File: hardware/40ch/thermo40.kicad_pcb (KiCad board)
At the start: 4 copper layers, 250 x 145 mm, 731 parts, among them J1001 PT100 1-2 (A B C), J1002 PT100 3 (A B C), J101 TC CH1-4, J102 TC CH5-8, J201 TC CH9-12, J202 TC CH13-16, J301 TC CH17-20, J302 TC CH21-24, J401 ENGINE REF FEED/SENSE, J501 AVR ISP, J502 LCD 20x4 HEADER, J503 PANEL BUTTONS, J601 24V IN, J701 TRIP C-NO-NC, J702 ALM C-NO-NC, J703 RS485 A B GND, J801 TC CH25-28, J802 TC CH29-32, J901 TC CH33-36, J902 TC CH37-40, K701 G6K-2F-Y DC5, K702 G6K-2F-Y DC5, Q401 2N7002, Q402 MMBT3906, Q701 2N7002, Q702 2N7002, SW501 UP, SW502 DOWN, SW503 SET, SW504 ESC, SW505 ACK, U1001 AD7124-8BCPZ, U101 AD7124-8BCPZ, U102 TMP126DCKR, U103 TMP126DCKR, U201 AD7124-8BCPZ, U202 TMP126DCKR, U203 TMP126DCKR, U301 AD7124-8BCPZ, U302 TMP126DCKR, U303 TMP126DCKR, U401 B0505S-1WR2, U402 LP2985IM5X-3.3, U403 CA-IS3761HW, U404 CA-IS3761HW, U406 REF3030AIDBZR, U407 MCP6001T-I/OT, U408 TLV7031DBVR, U409 TL431, U410 74HC154, U411 74LVC1G125, U501 ATmega1284P-AU, U601 LM5164DDAR, U703 ADM2587EBRWZ, U801 AD7124-8BCPZ, U802 TMP126DCKR, U803 TMP126DCKR, U901 AD7124-8BCPZ, U902 TMP126DCKR, U903 TMP126DCKR, Y501 8MHz

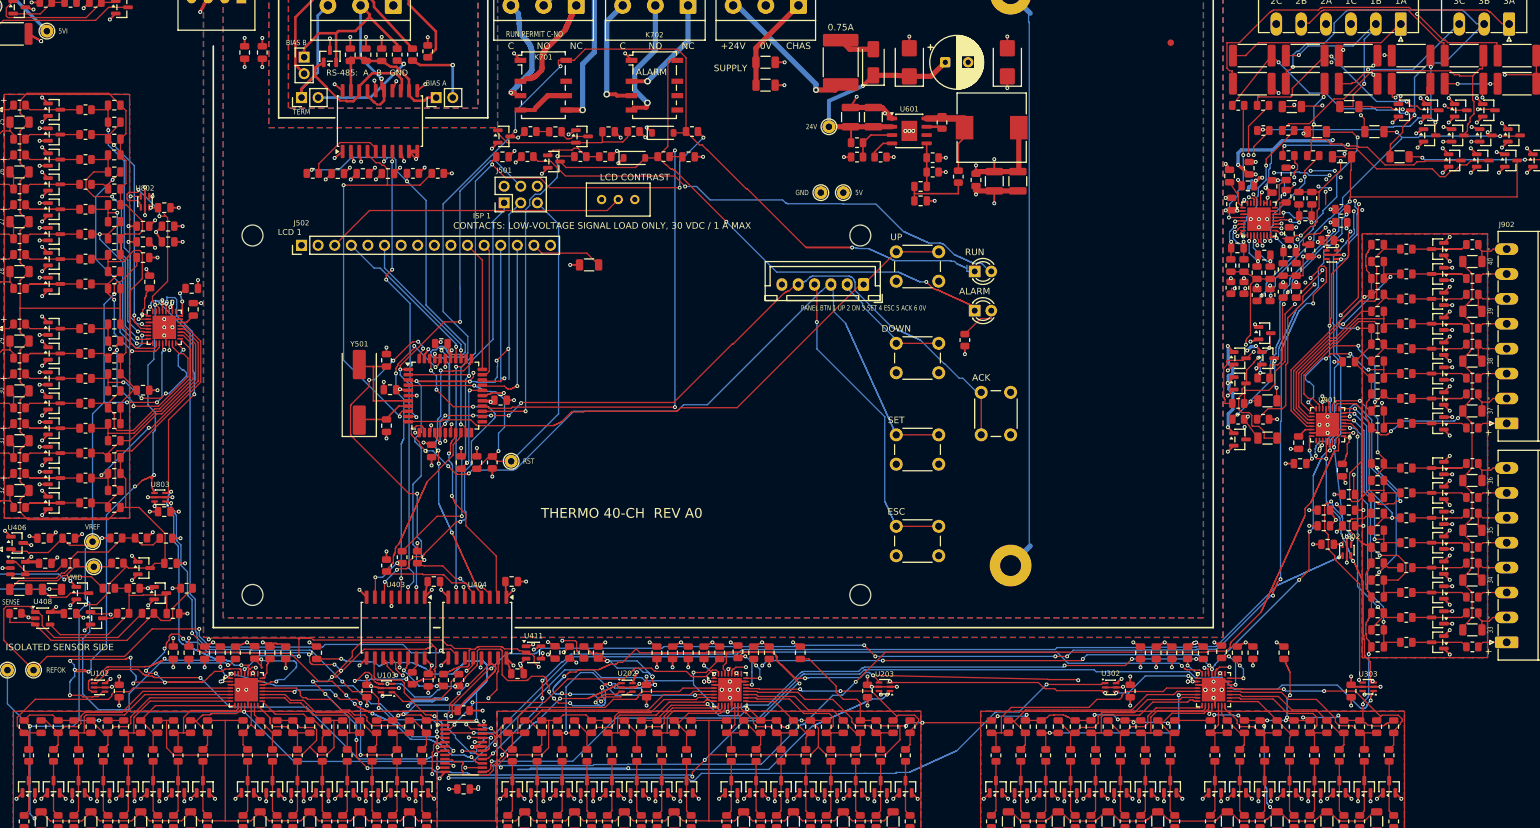
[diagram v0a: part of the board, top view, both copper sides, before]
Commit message: 40ch REV A0: drill-hole overlaps and via holes in SMD lands fixed (Astra re-review)
Sol round 11: hole pairs under 0.25 mm 19 -> 0 (KiCad hole_to_hole/holes_co_located 0),
via hole to small SMD land under 0.10 mm 61 -> 0, SAC/SBC partly shortened. DRC 0/0/0,
pincaps 0. Release 40ch-reva0-20261019-040422-9bed30; 024508 archived.

Co-Authored-By: Claude Opus 5.5 <noreply@anthropic.com>
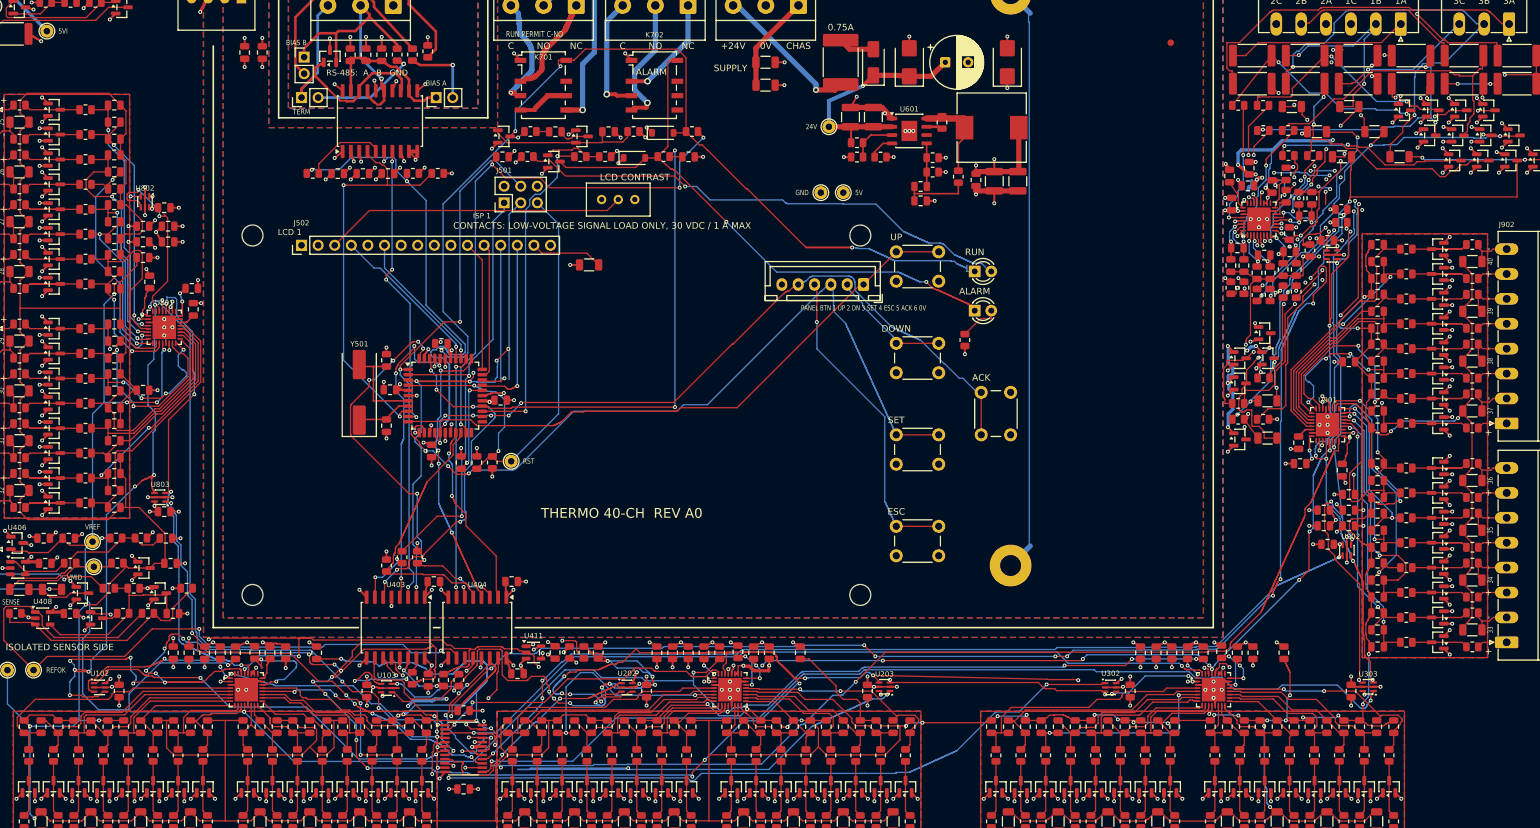
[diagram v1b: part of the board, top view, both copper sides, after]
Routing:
- net +3V3_ISO: track 352.1 -> 363.3 mm, vias 185 -> 180
- net /RTD_1/RTD1_SAC: track 66.1 -> 61.5 mm, vias 3 -> 6
- net GND_ISO: track 456.6 -> 460.3 mm, vias 239 -> 230
- net RTD3_SP: track 12.5 -> 15.5 mm
- net /RTD_1/RTD2_SBC: track 54.9 -> 57.4 mm
- net DOUT_ISO: track 506.8 -> 508.9 mm, vias 36 -> 30
- net SCLK_ISO: track 648.2 -> 650.0 mm
- net CSA1: track 44.7 -> 46.3 mm
- net /RTD_1/RTD1_C: track 5.93 -> 7.48 mm
- net V_BIAS: track 1024.9 -> 1026.4 mm, vias 39 -> 38
- net CSA0: track 44.7 -> 46.1 mm
- net RTD3_SN: track 13.3 -> 14.7 mm
- net /RTD_1/RTD4_SBC: track 44.7 -> 45.5 mm
- net /RTD_1/RTD2_XA: track 39.9 -> 40.7 mm
- net +5V: track 65.0 -> 65.8 mm
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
